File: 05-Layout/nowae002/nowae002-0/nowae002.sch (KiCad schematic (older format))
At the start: 55 parts, among them J1 SMALL_JUMPER, J2 SMALL_JUMPER, J3 SMALL_JUMPER, P1 USB_A_90, Q1 IRLML6402, U1 FT230XQ, U2 TPS62152, U3 RN4870

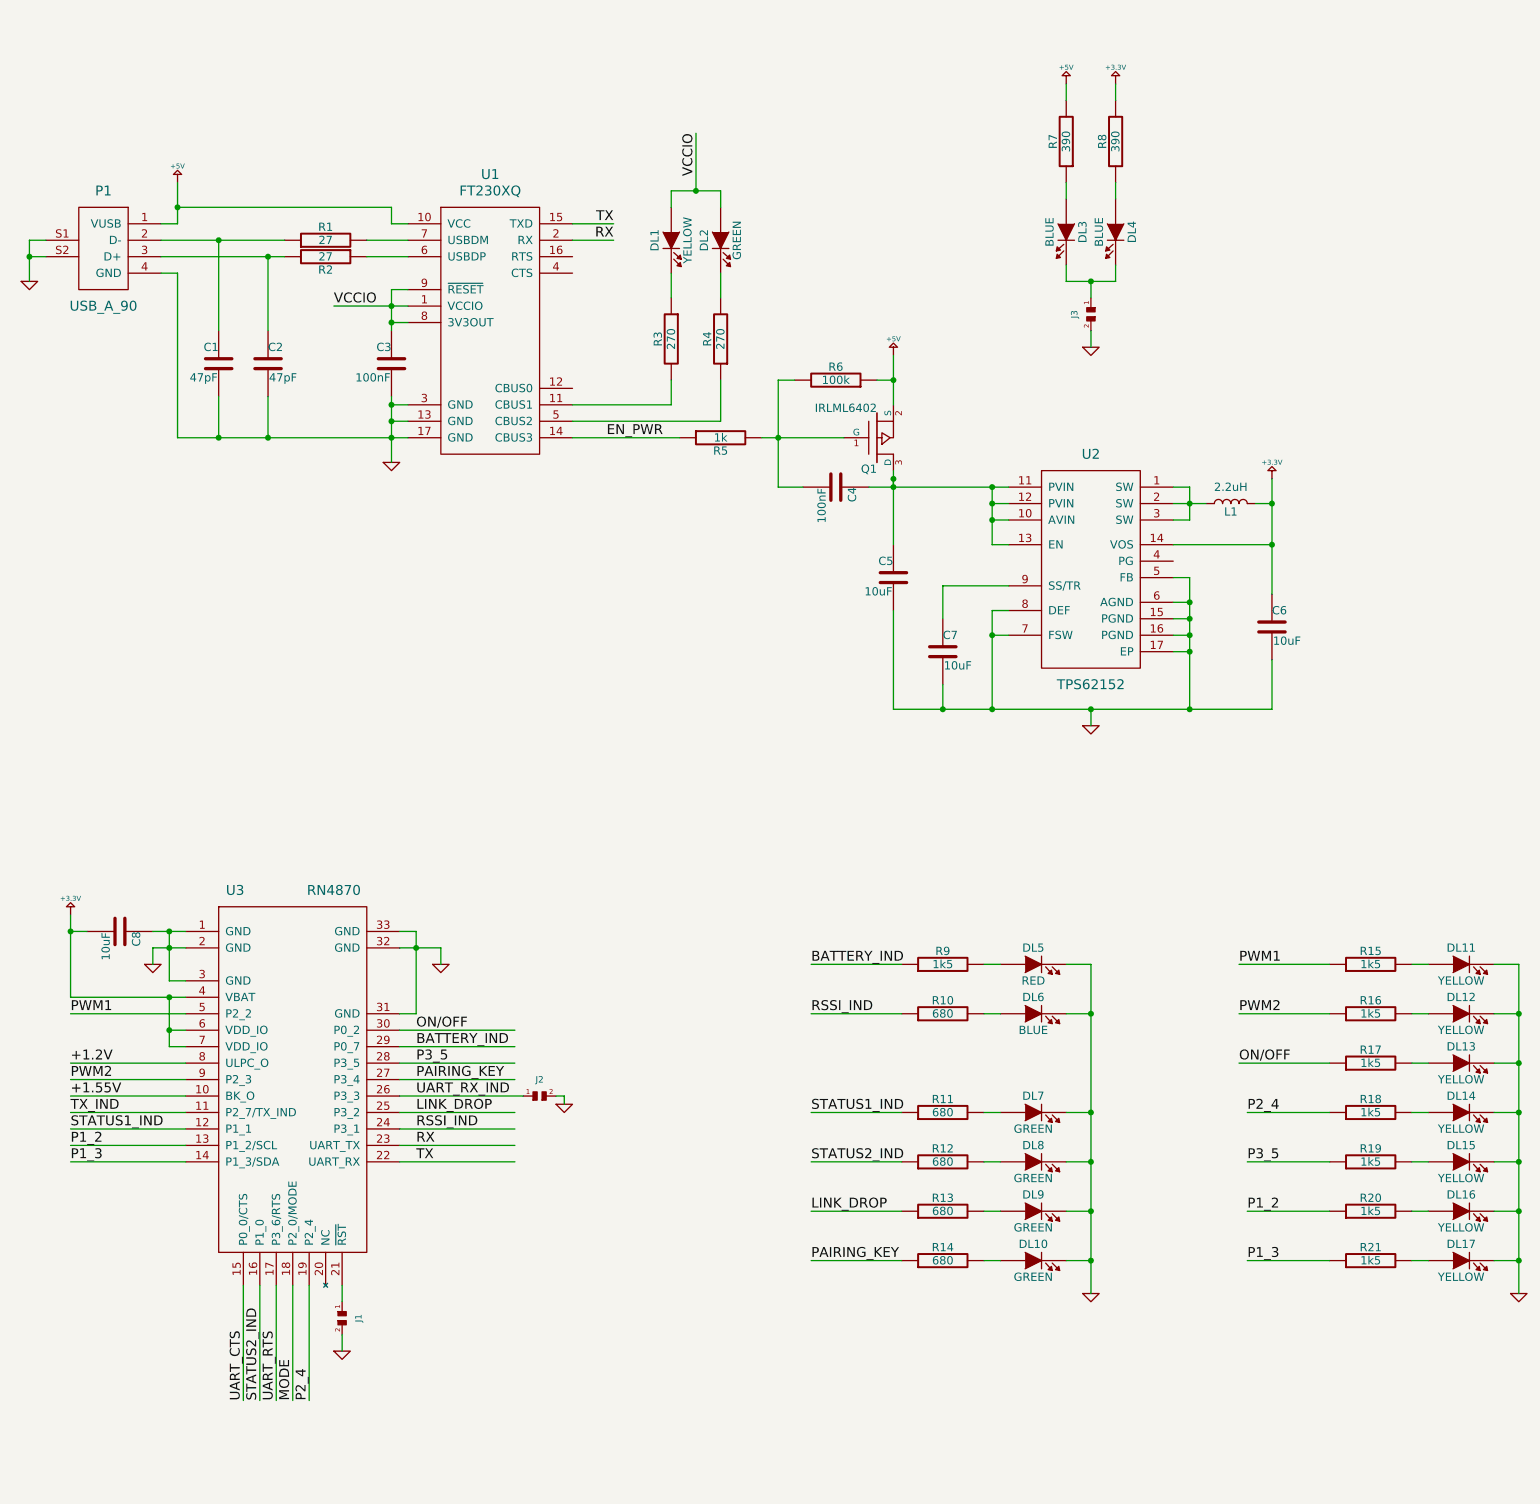
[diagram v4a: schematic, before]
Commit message: Added jumper for setting mode (RN4870) in nowae002
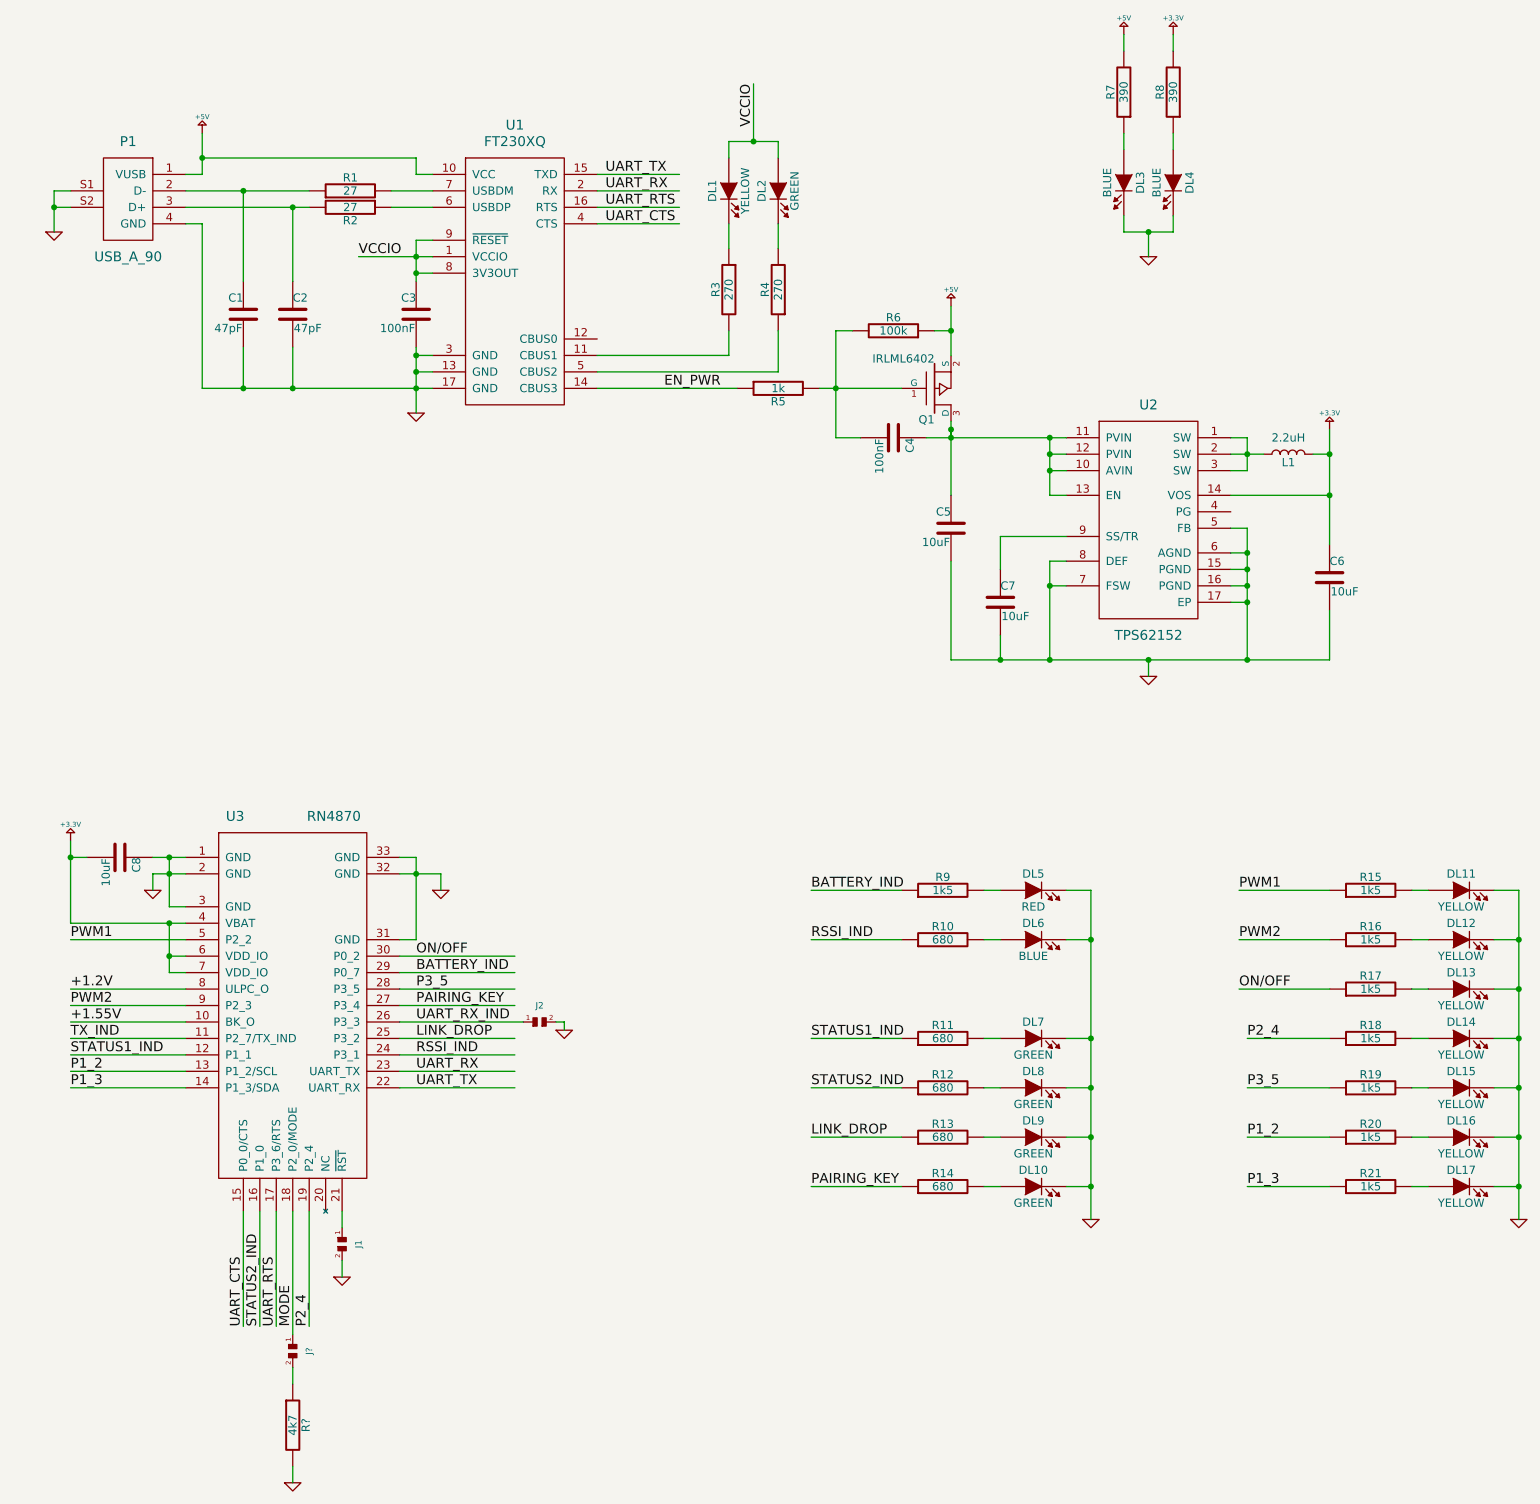
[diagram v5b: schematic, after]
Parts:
- removed J3: SMALL_JUMPER, MISC:JUMPERSMD-2, symbol SMALL_JUMPER
- added J?: SMALL_JUMPER, MISC:JUMPERSMD-2, symbol SMALL_JUMPER
- added R?: 4k7, symbol RESISTOR
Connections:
- net labels added: UART_RX, UART_TX
- net labels removed: RX, TX
- wire segments 167 -> 170
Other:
- moved on the sheet: C1, C2, C3, C4, C5, C6, C7, C8, DL1, DL10, DL11, DL12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

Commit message: Minor fixes (nowae002)
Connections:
- net labels added: RESET
- wire segments 170 -> 231
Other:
- moved on the sheet: C8, J1, J2, J?, R?, U3
